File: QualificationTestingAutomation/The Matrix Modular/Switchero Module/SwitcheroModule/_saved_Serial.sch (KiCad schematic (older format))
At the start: 13 parts, among them IC1 MAX3109ETJ+, Q2 2N7002DW

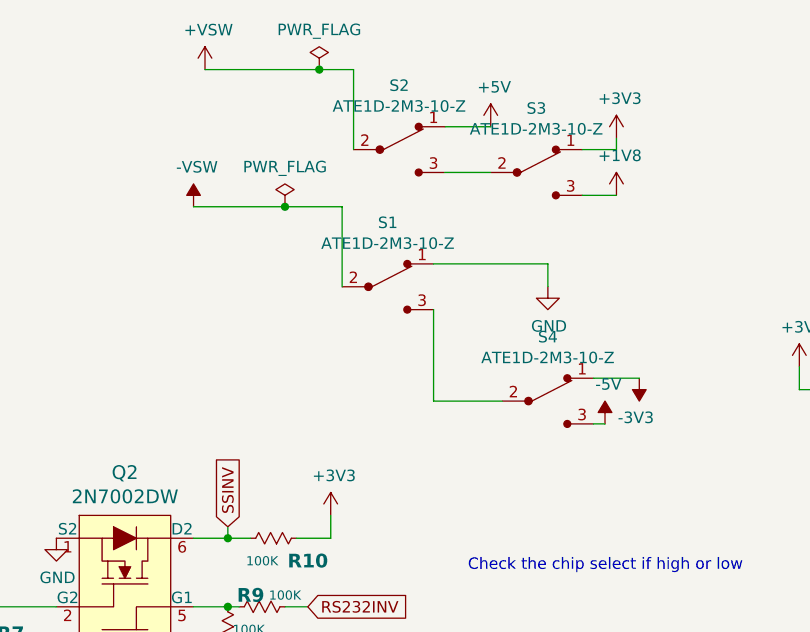
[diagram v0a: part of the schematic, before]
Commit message: Reefero Module PCB design
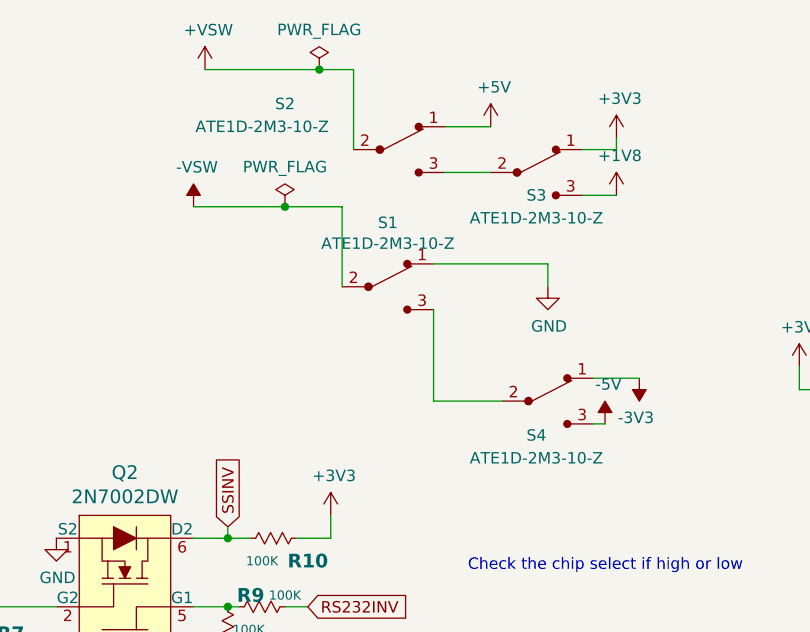
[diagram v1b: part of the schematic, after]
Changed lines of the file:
@@
 AR Path="/5C8DF48C/5CB40D46" Ref="S?"  Part="1"
 AR Path="/5C90F514/5CB40D46" Ref="S2"  Part="1"
-F 0 "S2" H 3700 2880 50  0000 C CNN
-F 1 "ATE1D-2M3-10-Z" H 3700 2789 50  0000 C CNN
+F 0 "S2" H 3200 2800 50  0000 C CNN
+F 1 "ATE1D-2M3-10-Z" H 3100 2700 50  0000 C CNN
 F 2 "Button_Switch_SMD:SW_SPDT_CK-JS102011SAQN" H 3900 2800 50  0001 L CNN
 F 3 "https://www.nidec-copal-electronics.com/e/catalog/switch/ate.pdf" H 3900 2900 60  0001 L CNN
@@
 AR Path="/5C8DF48C/5CB40DA3" Ref="S?"  Part="1"
 AR Path="/5C90F514/5CB40DA3" Ref="S4"  Part="1"
-F 0 "S4" H 4350 3980 50  0000 C CNN
-F 1 "ATE1D-2M3-10-Z" H 4350 3889 50  0000 C CNN
+F 0 "S4" H 4300 3550 50  0000 C CNN
+F 1 "ATE1D-2M3-10-Z" H 4300 3450 50  0000 C CNN
 F 2 "Button_Switch_SMD:SW_SPDT_CK-JS102011SAQN" H 4550 3900 50  0001 L CNN
 F 3 "https://www.nidec-copal-electronics.com/e/catalog/switch/ate.pdf" H 4550 4000 60  0001 L CNN
@@
 AR Path="/5C8DF48C/5CB40DBC" Ref="S?"  Part="1"
 AR Path="/5C90F514/5CB40DBC" Ref="S3"  Part="1"
-F 0 "S3" H 4300 2980 50  0000 C CNN
-F 1 "ATE1D-2M3-10-Z" H 4300 2889 50  0000 C CNN
+F 0 "S3" H 4300 2600 50  0000 C CNN
+F 1 "ATE1D-2M3-10-Z" H 4300 2500 50  0000 C CNN
 F 2 "Button_Switch_SMD:SW_SPDT_CK-JS102011SAQN" H 4500 2900 50  0001 L CNN
 F 3 "https://www.nidec-copal-electronics.com/e/catalog/switch/ate.pdf" H 4500 3000 60  0001 L CNN
